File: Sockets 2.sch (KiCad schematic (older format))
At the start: 17 parts, among them J18 TABLE SENSOR, J19 PHOTO SENSOR EMITER, J20 PHOTO SENSOR RECEIVER, Q5 BC817, Q6 BC817

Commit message: Shematic almost finished, BOM in KiCad 3/4 finished
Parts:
- C60: renamed from 1nF1; value C -> 1nF; footprint (none) -> Capacitor_SMD:C_0603_1608Metric
- C61: renamed from 1nF2; value C -> 1nF; footprint (none) -> Capacitor_SMD:C_0603_1608Metric
- D27, D28: Cena (none) -> 0.14905; Link (none) -> https://www.tme.eu/pl/details/1n4448ws-7-f/diody-uniwersaln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; Model (none) -> 1N4448WS-7-F; Opis (none) -> Dioda: prostownicza; SMD; 75V; 0,25A; 4ns;; Producent (none) -> DIODES INCORPORATED; Typ (none) -> SMD
- F4, F5: Cena (none) -> 0.3763; Link (none) -> https://www.tme.eu/pl/details/sn010-60/bezpieczniki-polimer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; Model (none) -> SN010-60; Opis (none) -> Bezpiecznik: polimerowy PTC; 100mA; Obud: 1206; Producent (none) -> ECE; Typ (none) -> SMD
- J18, J20: footprint Connector_JST:JST_PH_B2B-PH-K_1x03_P2.00mm_Vertical -> Connector_JST:JST_PH_B3B-PH-K_1x03_P2.00mm_Vertical; Cena (none) -> 0.59599; Link (none) -> https://www.tme.eu/pl/details/b3b-ph-k-s/zlacza-sygnalowe-r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; Model (none) -> B3B-PH-K-S; Opis (none) -> Gniazdo; przewód-płytka; męskie; PH; 2mm; PIN: 3; THT; 100V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; Producent (none) -> JST; Typ (none) -> THT
- J19: Cena (none) -> 0.47429; Link (none) -> https://www.tme.eu/pl/details/b2b-ph-k-s/zlacza-sygnalowe-r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; Model (none) -> B2B-PH-K-S; Opis (none) -> Gniazdo; przewód-płytka; męskie; PH; 2mm; PIN: 2; THT; 100V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; Producent (none) -> JST; Typ (none) -> THT
- renumbered R50 to R49, R53 to R50, R54 to R52, R49 to R53, R52 to R54
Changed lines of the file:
@@
 F 0 "J18" H 1122 1724 50  0000 R CNN
 F 1 "TABLE SENSOR" H 1350 1900 50  0000 R CNN
-F 2 "Connector_JST:JST_PH_B2B-PH-K_1x03_P2.00mm_Vertical" H 1150 1700 50  0001 C CNN
+F 2 "Connector_JST:JST_PH_B3B-PH-K_1x03_P2.00mm_Vertical" H 1150 1700 50  0001 C CNN
 F 3 "~" H 1150 1700 50  0001 C CNN
+F 4 "0.59599" H 1150 1700 50  0001 C CNN "Cena"
+F 5 "https://www.tme.eu/pl/details/b3b-ph-k-s/zlacza-sygnalowe-raster-2-00mm/jst/" H 1150 1700 50  0001 C CNN "Link"
+F 6 "B3B-PH-K-S" H 1150 1700 50  0001 C CNN "Model"
+F 7 "Gniazdo; przewód-płytka; męskie; PH; 2mm; PIN: 3; THT; 100V; 2A" H 1150 1700 50  0001 C CNN "Opis"
+F 8 "JST" H 1150 1700 50  0001 C CNN "Producent"
+F 9 "THT" H 1150 1700 50  0001 C CNN "Typ"
 	1    1150 1700
 	1    0    0    -1
@@
 P 2450 1050
 AR Path="/5E07245F/5E173AD0" Ref="#PWR?"  Part="1"
-AR Path="/5E858220/5E173AD0" Ref="#PWR0131"  Part="1"
-F 0 "#PWR0131" H 2250 900 50  0001 C CNN
+AR Path="/5E858220/5E173AD0" Ref="#PWR0133"  Part="1"
+F 0 "#PWR0133" H 2250 900 50  0001 C CNN
 F 1 "VS" H 2467 1223 50  0000 C CNN
 F 2 "" H 2450 1050 50  0001 C CNN
@@
 F 2 "Fuse:Fuse_1206_3216Metric" H 2200 1050 50  0001 L CNN
 F 3 "~" H 2150 1250 50  0001 C CNN
+F 4 "0.3763" H 2150 1250 50  0001 C CNN "Cena"
+F 5 "https://www.tme.eu/pl/details/sn010-60/bezpieczniki-polimerowe-smd/ece/" H 2150 1250 50  0001 C CNN "Link"
+F 6 "SN010-60" H 2150 1250 50  0001 C CNN "Model"
+F 7 "Bezpiecznik: polimerowy PTC; 100mA; Obud: 1206" H 2150 1250 50  0001 C CNN "Opis"
+F 8 "ECE" H 2150 1250 50  0001 C CNN "Producent"
+F 9 "SMD" H 2150 1250 50  0001 C CNN "Typ"
 	1    2150 1250
 	0    1    1    0
@@
 P 1500 1900
 AR Path="/5E07245F/5E17A8E3" Ref="#PWR?"  Part="1"
-AR Path="/5E858220/5E17A8E3" Ref="#PWR0133"  Part="1"
-F 0 "#PWR0133" H 1500 1650 50  0001 C CNN
+AR Path="/5E858220/5E17A8E3" Ref="#PWR0131"  Part="1"
+F 0 "#PWR0131" H 1500 1650 50  0001 C CNN
 F 1 "GND" H 1505 1727 50  0000 C CNN
 F 2 "" H 1500 1900 50  0001 C CNN
@@
 P 1800 1450
 AR Path="/5E07245F/5E17BAB2" Ref="R?"  Part="1"
-AR Path="/5E858220/5E17BAB2" Ref="R50"  Part="1"
-F 0 "R50" H 1650 1500 50  0000 C CNN
+AR Path="/5E858220/5E17BAB2" Ref="R49"  Part="1"
+F 0 "R49" H 1650 1500 50  0000 C CNN
 F 1 "10kΩ" H 1650 1400 50  0000 C CNN
 F 2 "Resistor_SMD:R_0603_1608Metric" V 1730 1450 50  0001 C CNN
@@
 F 2 "Diode_SMD:D_SOD-323" H 2650 1900 50  0001 C CNN
 F 3 "~" H 2650 1900 50  0001 C CNN
+F 4 "0.14905" H 2650 1900 50  0001 C CNN "Cena"
+F 5 "https://www.tme.eu/pl/details/1n4448ws-7-f/diody-uniwersalne-smd/diodes-incorporated/" H 2650 1900 50  0001 C CNN "Link"
+F 6 "1N4448WS-7-F" H 2650 1900 50  0001 C CNN "Model"
+F 7 "Dioda: prostownicza; SMD; 75V; 0,25A; 4ns;" H 2650 1900 50  0001 C CNN "Opis"
+F 8 "DIODES INCORPORATED" H 2650 1900 50  0001 C CNN "Producent"
+F 9 "SMD" H 2650 1900 50  0001 C CNN "Typ"
 	1    2650 1900
 	0    1    1    0
@@
 P 3000 2150
 AR Path="/5E07245F/5E18427F" Ref="#PWR?"  Part="1"
-AR Path="/5E858220/5E18427F" Ref="#PWR0134"  Part="1"
-F 0 "#PWR0134" H 3000 1900 50  0001 C CNN
+AR Path="/5E858220/5E18427F" Ref="#PWR0136"  Part="1"
+F 0 "#PWR0136" H 3000 1900 50  0001 C CNN
 F 1 "GND" H 3005 1977 50  0000 C CNN
 F 2 "" H 3000 2150 50  0001 C CNN
@@
 P 3000 1250
 AR Path="/5E07245F/5E185B5B" Ref="R?"  Part="1"
-AR Path="/5E858220/5E185B5B" Ref="R49"  Part="1"
-F 0 "R49" H 2850 1300 50  0000 C CNN
+AR Path="/5E858220/5E185B5B" Ref="R53"  Part="1"
+F 0 "R53" H 2850 1300 50  0000 C CNN
 F 1 "10kΩ" H 2850 1200 50  0000 C CNN
 F 2 "Resistor_SMD:R_0603_1608Metric" V 2930 1250 50  0001 C CNN
@@
 $EndComp
 $Comp
-L power:+3.3V #PWR0132
+L power:+3.3V #PWR0135
 U 1 1 5E187914
 P 3000 1050
-F 0 "#PWR0132" H 3000 900 50  0001 C CNN
+F 0 "#PWR0135" H 3000 900 50  0001 C CNN
 F 1 "+3.3V" H 3015 1223 50  0000 C CNN
 F 2 "" H 3000 1050 50  0001 C CNN
@@
 NPN NC
 $Comp
-L Device:C 1nF1
+L Device:C C60
 U 1 1 5E189FA4
 P 3550 1700
-F 0 "1nF1" H 3665 1746 50  0000 L CNN
-F 1 "C" H 3665 1655 50  0000 L CNN
-F 2 "" H 3588 1550 50  0001 C CNN
+F 0 "C60" H 3665 1746 50  0000 L CNN
+F 1 "1nF" H 3665 1655 50  0000 L CNN
+F 2 "Capacitor_SMD:C_0603_1608Metric" H 3588 1550 50  0001 C CNN
 F 3 "~" H 3550 1700 50  0001 C CNN
 	1    3550 1700
@@
 F 0 "J20" H 1372 3874 50  0000 R CNN
 F 1 "PHOTO SENSOR RECEIVER" H 1600 4050 50  0000 R CNN
-F 2 "Connector_JST:JST_PH_B2B-PH-K_1x03_P2.00mm_Vertical" H 1400 3850 50  0001 C CNN
+F 2 "Connector_JST:JST_PH_B3B-PH-K_1x03_P2.00mm_Vertical" H 1400 3850 50  0001 C CNN
 F 3 "~" H 1400 3850 50  0001 C CNN
+F 4 "0.59599" H 1400 3850 50  0001 C CNN "Cena"
+F 5 "https://www.tme.eu/pl/details/b3b-ph-k-s/zlacza-sygnalowe-raster-2-00mm/jst/" H 1400 3850 50  0001 C CNN "Link"
+F 6 "B3B-PH-K-S" H 1400 3850 50  0001 C CNN "Model"
+F 7 "Gniazdo; przewód-płytka; męskie; PH; 2mm; PIN: 3; THT; 100V; 2A" H 1400 3850 50  0001 C CNN "Opis"
+F 8 "JST" H 1400 3850 50  0001 C CNN "Producent"
+F 9 "THT" H 1400 3850 50  0001 C CNN "Typ"
 	1    1400 3850
 	1    0    0    -1
@@
 P 2550 2850
 AR Path="/5E07245F/5E1B90F7" Ref="#PWR?"  Part="1"
-AR Path="/5E858220/5E1B90F7" Ref="#PWR0135"  Part="1"
-F 0 "#PWR0135" H 2350 2700 50  0001 C CNN
+AR Path="/5E858220/5E1B90F7" Ref="#PWR0134"  Part="1"
+F 0 "#PWR0134" H 2350 2700 50  0001 C CNN
 F 1 "VS" H 2567 3023 50  0000 C CNN
 F 2 "" H 2550 2850 50  0001 C CNN
@@
 F 2 "Fuse:Fuse_1206_3216Metric" H 2250 2800 50  0001 L CNN
 F 3 "~" H 2200 3000 50  0001 C CNN
+F 4 "0.3763" H 2200 3000 50  0001 C CNN "Cena"
+F 5 "https://www.tme.eu/pl/details/sn010-60/bezpieczniki-polimerowe-smd/ece/" H 2200 3000 50  0001 C CNN "Link"
+F 6 "SN010-60" H 2200 3000 50  0001 C CNN "Model"
+F 7 "Bezpiecznik: polimerowy PTC; 100mA; Obud: 1206" H 2200 3000 50  0001 C CNN "Opis"
+F 8 "ECE" H 2200 3000 50  0001 C CNN "Producent"
+F 9 "SMD" H 2200 3000 50  0001 C CNN "Typ"
 	1    2200 3000
 	0    1    1    0
@@
 P 1700 4050
 AR Path="/5E07245F/5E1B910F" Ref="#PWR?"  Part="1"
-AR Path="/5E858220/5E1B910F" Ref="#PWR0137"  Part="1"
-F 0 "#PWR0137" H 1700 3800 50  0001 C CNN
+AR Path="/5E858220/5E1B910F" Ref="#PWR0132"  Part="1"
+F 0 "#PWR0132" H 1700 3800 50  0001 C CNN
 F 1 "GND" H 1705 3877 50  0000 C CNN
 F 2 "" H 1700 4050 50  0001 C CNN
@@
 P 2050 3450
 AR Path="/5E07245F/5E1B911B" Ref="R?"  Part="1"
-AR Path="/5E858220/5E1B911B" Ref="R53"  Part="1"
-F 0 "R53" H 2150 3500 50  0000 C CNN
+AR Path="/5E858220/5E1B911B" Ref="R50"  Part="1"
+F 0 "R50" H 2150 3500 50  0000 C CNN
 F 1 "10kΩ" H 2200 3400 50  0000 C CNN
 F 2 "Resistor_SMD:R_0603_1608Metric" V 1980 3450 50  0001 C CNN
@@
 P 2350 3850
 AR Path="/5E07245F/5E1B9135" Ref="R?"  Part="1"
-AR Path="/5E858220/5E1B9135" Ref="R54"  Part="1"
-F 0 "R54" V 2150 3850 50  0000 C CNN
+AR Path="/5E858220/5E1B9135" Ref="R52"  Part="1"
+F 0 "R52" V 2150 3850 50  0000 C CNN
 F 1 "33kΩ" V 2250 3850 50  0000 C CNN
 F 2 "Resistor_SMD:R_0603_1608Metric" V 2280 3850 50  0001 C CNN
@@
 F 2 "Diode_SMD:D_SOD-323" H 2900 4050 50  0001 C CNN
 F 3 "~" H 2900 4050 50  0001 C CNN
+F 4 "0.14905" H 2900 4050 50  0001 C CNN "Cena"
+F 5 "https://www.tme.eu/pl/details/1n4448ws-7-f/diody-uniwersalne-smd/diodes-incorporated/" H 2900 4050 50  0001 C CNN "Link"
+F 6 "1N4448WS-7-F" H 2900 4050 50  0001 C CNN "Model"
+F 7 "Dioda: prostownicza; SMD; 75V; 0,25A; 4ns;" H 2900 4050 50  0001 C CNN "Opis"
+F 8 "DIODES INCORPORATED" H 2900 4050 50  0001 C CNN "Producent"
+F 9 "SMD" H 2900 4050 50  0001 C CNN "Typ"
 	1    2900 4050
 	0    1    1    0
@@
 P 3250 3400
 AR Path="/5E07245F/5E1B915B" Ref="R?"  Part="1"
-AR Path="/5E858220/5E1B915B" Ref="R52"  Part="1"
-F 0 "R52" H 3100 3450 50  0000 C CNN
+AR Path="/5E858220/5E1B915B" Ref="R54"  Part="1"
+F 0 "R54" H 3100 3450 50  0000 C CNN
 F 1 "10kΩ" H 3100 3350 50  0000 C CNN
 F 2 "Resistor_SMD:R_0603_1608Metric" V 3180 3400 50  0001 C CNN
@@
 $EndComp
 $Comp
-L power:+3.3V #PWR0136
+L power:+3.3V #PWR0137
 U 1 1 5E1B9165
 P 3250 3200
-F 0 "#PWR0136" H 3250 3050 50  0001 C CNN
+F 0 "#PWR0137" H 3250 3050 50  0001 C CNN
 F 1 "+3.3V" H 3265 3373 50  0000 C CNN
 F 2 "" H 3250 3200 50  0001 C CNN
@@
 NPN NC
 $Comp
-L Device:C 1nF2
+L Device:C C61
 U 1 1 5E1B9175
 P 3800 3850
-F 0 "1nF2" H 3915 3896 50  0000 L CNN
-F 1 "C" H 3915 3805 50  0000 L CNN
-F 2 "" H 3838 3700 50  0001 C CNN
+F 0 "C61" H 3915 3896 50  0000 L CNN
+F 1 "1nF" H 3915 3805 50  0000 L CNN
+F 2 "Capacitor_SMD:C_0603_1608Metric" H 3838 3700 50  0001 C CNN
 F 3 "~" H 3800 3850 50  0001 C CNN
 	1    3800 3850
@@
 F 2 "Connector_JST:JST_PH_B2B-PH-K_1x02_P2.00mm_Vertical" H 1400 3000 50  0001 C CNN
 F 3 "~" H 1400 3000 50  0001 C CNN
+F 4 "0.47429" H 1400 3000 50  0001 C CNN "Cena"
+F 5 "https://www.tme.eu/pl/details/b2b-ph-k-s/zlacza-sygnalowe-raster-2-00mm/jst/" H 1400 3000 50  0001 C CNN "Link"
+F 6 "B2B-PH-K-S" H 1400 3000 50  0001 C CNN "Model"
+F 7 "Gniazdo; przewód-płytka; męskie; PH; 2mm; PIN: 2; THT; 100V; 2A" H 1400 3000 50  0001 C CNN "Opis"
+F 8 "JST" H 1400 3000 50  0001 C CNN "Producent"
+F 9 "THT" H 1400 3000 50  0001 C CNN "Typ"
 	1    1400 3000
 	1    0    0    -1

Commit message: BOM in KiCad almost finished, genereated NETLIST, create PCB
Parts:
- C60, C61: Cena (none) -> 0.05563; Link (none) -> https://www.tme.eu/pl/details/cl10b102kb8nnnc/kondensatory-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; Model (none) -> CL10B102KB8NNNC; Opis (none) -> Kondensator: ceramiczny; MLCC; 1nF; 50V; X7R; ±10%; SMD; 06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; Producent (none) -> SAMSUNG; Typ (none) -> SMD
- Q5, Q6: Cena (none) -> 0.1189; Link (none) -> https://www.tme.eu/pl/details/bc817.215/tranzystory-npn-smd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; Model (none) -> BC817.215; Opis (none) -> Tranzystor: NPN; bipolarny; 45V; 0,5A; 250mW; SOT23; Producent (none) -> NEXPERIA; Typ (none) -> SMD
- R49, R50, R53, R54: Cena (none) -> 0.03622; Link (none) -> https://www.tme.eu/pl/details/smd0603-10k-1%25/rezystory-sm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; Model (none) -> 0603SAF1002T5E; Opis (none) -> Rezystor: thick film; SMD; 0603; 10kΩ; 0,1W; ±1%; -55÷155°C; Producent (none) -> ROYAL OHM; Typ (none) -> SMD
- R51, R52: Cena (none) -> 0.04651; Typ (none) -> SMD
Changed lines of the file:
@@
 F 2 "Resistor_SMD:R_0603_1608Metric" V 1730 1450 50  0001 C CNN
 F 3 "~" H 1800 1450 50  0001 C CNN
+F 4 "0.03622" H 1800 1450 50  0001 C CNN "Cena"
+F 5 "https://www.tme.eu/pl/details/smd0603-10k-1%25/rezystory-smd-0603/royal-ohm/0603saf1002t5e/" H 1800 1450 50  0001 C CNN "Link"
+F 6 "0603SAF1002T5E" H 1800 1450 50  0001 C CNN "Model"
+F 7 "Rezystor: thick film; SMD; 0603; 10kΩ; 0,1W; ±1%; -55÷155°C" H 1800 1450 50  0001 C CNN "Opis"
+F 8 "ROYAL OHM" H 1800 1450 50  0001 C CNN "Producent"
+F 9 "SMD" H 1800 1450 50  0001 C CNN "Typ"
 	1    1800 1450
 	1    0    0    -1
@@
 F 2 "Package_TO_SOT_SMD:SOT-23" H 3100 1625 50  0001 L CIN
 F 3 "http://www.fairchildsemi.com/ds/BC/BC817.pdf" H 2900 1700 50  0001 L CNN
+F 4 "0.1189" H 2900 1700 50  0001 C CNN "Cena"
+F 5 "https://www.tme.eu/pl/details/bc817.215/tranzystory-npn-smd/nexperia/" H 2900 1700 50  0001 C CNN "Link"
+F 6 "BC817.215" H 2900 1700 50  0001 C CNN "Model"
+F 7 "Tranzystor: NPN; bipolarny; 45V; 0,5A; 250mW; SOT23" H 2900 1700 50  0001 C CNN "Opis"
+F 8 "NEXPERIA" H 2900 1700 50  0001 C CNN "Producent"
+F 9 "SMD" H 2900 1700 50  0001 C CNN "Typ"
 	1    2900 1700
 	1    0    0    -1
@@
 F 2 "Resistor_SMD:R_0603_1608Metric" V 2030 1700 50  0001 C CNN
 F 3 "~" H 2100 1700 50  0001 C CNN
+F 4 "0.04651" H 2100 1700 50  0001 C CNN "Cena"
+F 5 "SMD" H 2100 1700 50  0001 C CNN "Typ"
 	1    2100 1700
 	0    1    1    0
@@
 F 2 "Resistor_SMD:R_0603_1608Metric" V 2930 1250 50  0001 C CNN
 F 3 "~" H 3000 1250 50  0001 C CNN
+F 4 "0.03622" H 3000 1250 50  0001 C CNN "Cena"
+F 5 "https://www.tme.eu/pl/details/smd0603-10k-1%25/rezystory-smd-0603/royal-ohm/0603saf1002t5e/" H 3000 1250 50  0001 C CNN "Link"
+F 6 "0603SAF1002T5E" H 3000 1250 50  0001 C CNN "Model"
+F 7 "Rezystor: thick film; SMD; 0603; 10kΩ; 0,1W; ±1%; -55÷155°C" H 3000 1250 50  0001 C CNN "Opis"
+F 8 "ROYAL OHM" H 3000 1250 50  0001 C CNN "Producent"
+F 9 "SMD" H 3000 1250 50  0001 C CNN "Typ"
 	1    3000 1250
 	1    0    0    -1
@@
 F 2 "Capacitor_SMD:C_0603_1608Metric" H 3588 1550 50  0001 C CNN
 F 3 "~" H 3550 1700 50  0001 C CNN
+F 4 "0.05563" H 3550 1700 50  0001 C CNN "Cena"
+F 5 "https://www.tme.eu/pl/details/cl10b102kb8nnnc/kondensatory-mlcc-smd-0603/samsung/" H 3550 1700 50  0001 C CNN "Link"
+F 6 "CL10B102KB8NNNC" H 3550 1700 50  0001 C CNN "Model"
+F 7 "Kondensator: ceramiczny; MLCC; 1nF; 50V; X7R; ±10%; SMD; 0603" H 3550 1700 50  0001 C CNN "Opis"
+F 8 "SAMSUNG" H 3550 1700 50  0001 C CNN "Producent"
+F 9 "SMD" H 3550 1700 50  0001 C CNN "Typ"
 	1    3550 1700
 	1    0    0    -1
@@
 F 2 "Resistor_SMD:R_0603_1608Metric" V 1980 3450 50  0001 C CNN
 F 3 "~" H 2050 3450 50  0001 C CNN
+F 4 "0.03622" H 2050 3450 50  0001 C CNN "Cena"
+F 5 "https://www.tme.eu/pl/details/smd0603-10k-1%25/rezystory-smd-0603/royal-ohm/0603saf1002t5e/" H 2050 3450 50  0001 C CNN "Link"
+F 6 "0603SAF1002T5E" H 2050 3450 50  0001 C CNN "Model"
+F 7 "Rezystor: thick film; SMD; 0603; 10kΩ; 0,1W; ±1%; -55÷155°C" H 2050 3450 50  0001 C CNN "Opis"
+F 8 "ROYAL OHM" H 2050 3450 50  0001 C CNN "Producent"
+F 9 "SMD" H 2050 3450 50  0001 C CNN "Typ"
 	1    2050 3450
 	1    0    0    -1
@@
 F 2 "Package_TO_SOT_SMD:SOT-23" H 3350 3775 50  0001 L CIN
 F 3 "http://www.fairchildsemi.com/ds/BC/BC817.pdf" H 3150 3850 50  0001 L CNN
+F 4 "0.1189" H 3150 3850 50  0001 C CNN "Cena"
+F 5 "https://www.tme.eu/pl/details/bc817.215/tranzystory-npn-smd/nexperia/" H 3150 3850 50  0001 C CNN "Link"
+F 6 "BC817.215" H 3150 3850 50  0001 C CNN "Model"
+F 7 "Tranzystor: NPN; bipolarny; 45V; 0,5A; 250mW; SOT23" H 3150 3850 50  0001 C CNN "Opis"
+F 8 "NEXPERIA" H 3150 3850 50  0001 C CNN "Producent"
+F 9 "SMD" H 3150 3850 50  0001 C CNN "Typ"
 	1    3150 3850
 	1    0    0    -1
@@
 F 2 "Resistor_SMD:R_0603_1608Metric" V 2280 3850 50  0001 C CNN
 F 3 "~" H 2350 3850 50  0001 C CNN
+F 4 "0.04651" H 2350 3850 50  0001 C CNN "Cena"
+F 5 "SMD" H 2350 3850 50  0001 C CNN "Typ"
 	1    2350 3850
 	0    1    1    0
@@
 F 2 "Resistor_SMD:R_0603_1608Metric" V 3180 3400 50  0001 C CNN
 F 3 "~" H 3250 3400 50  0001 C CNN
+F 4 "0.03622" H 3250 3400 50  0001 C CNN "Cena"
+F 5 "https://www.tme.eu/pl/details/smd0603-10k-1%25/rezystory-smd-0603/royal-ohm/0603saf1002t5e/" H 3250 3400 50  0001 C CNN "Link"
+F 6 "0603SAF1002T5E" H 3250 3400 50  0001 C CNN "Model"
+F 7 "Rezystor: thick film; SMD; 0603; 10kΩ; 0,1W; ±1%; -55÷155°C" H 3250 3400 50  0001 C CNN "Opis"
+F 8 "ROYAL OHM" H 3250 3400 50  0001 C CNN "Producent"
+F 9 "SMD" H 3250 3400 50  0001 C CNN "Typ"
 	1    3250 3400
 	1    0    0    -1
@@
 F 2 "Capacitor_SMD:C_0603_1608Metric" H 3838 3700 50  0001 C CNN
 F 3 "~" H 3800 3850 50  0001 C CNN
+F 4 "0.05563" H 3800 3850 50  0001 C CNN "Cena"
+F 5 "https://www.tme.eu/pl/details/cl10b102kb8nnnc/kondensatory-mlcc-smd-0603/samsung/" H 3800 3850 50  0001 C CNN "Link"
+F 6 "CL10B102KB8NNNC" H 3800 3850 50  0001 C CNN "Model"
+F 7 "Kondensator: ceramiczny; MLCC; 1nF; 50V; X7R; ±10%; SMD; 0603" H 3800 3850 50  0001 C CNN "Opis"
+F 8 "SAMSUNG" H 3800 3850 50  0001 C CNN "Producent"
+F 9 "SMD" H 3800 3850 50  0001 C CNN "Typ"
 	1    3800 3850
 	1    0    0    -1

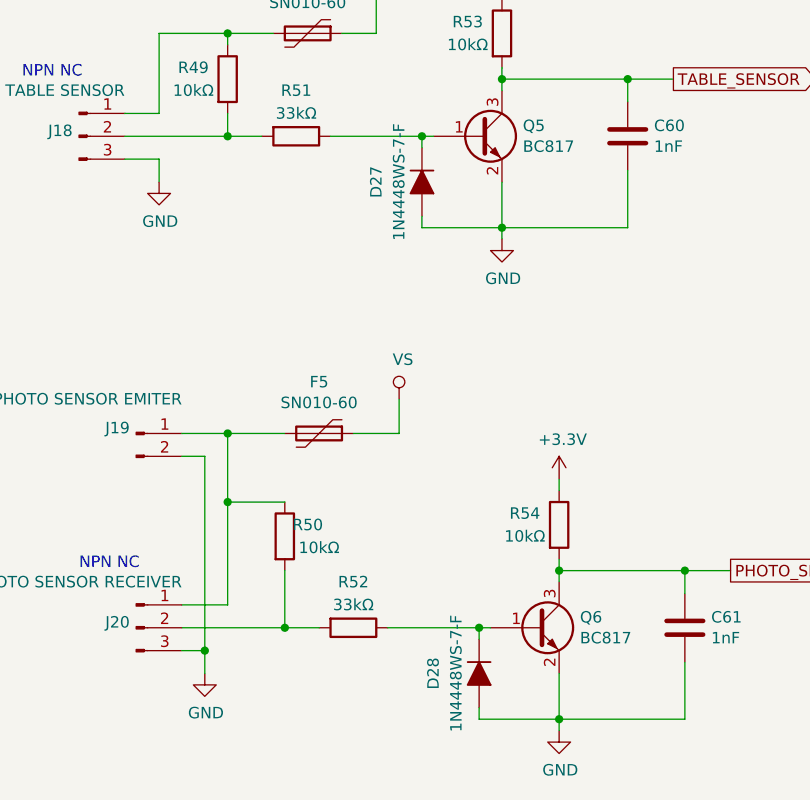
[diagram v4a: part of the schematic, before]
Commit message: Improve Emergency, Added TVS diodes
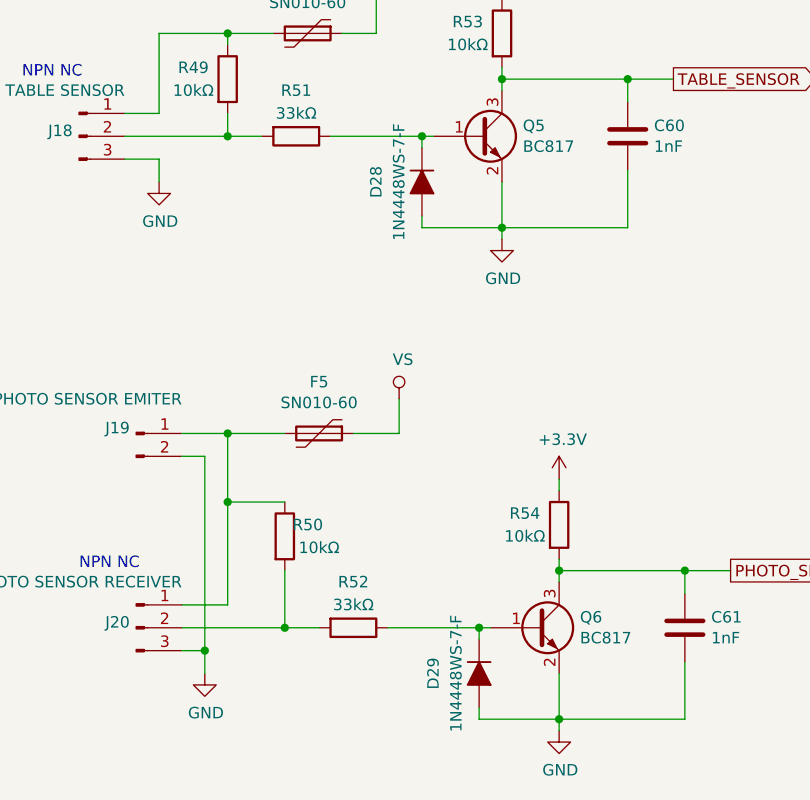
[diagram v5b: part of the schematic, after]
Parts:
- renumbered D27 to D28, D28 to D29
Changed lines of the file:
@@
 AR Path="/5E1018C2/5E182EF0" Ref="D?"  Part="1"
 AR Path="/5E91D7CC/5E182EF0" Ref="D?"  Part="1"
-AR Path="/5E858220/5E182EF0" Ref="D27"  Part="1"
-F 0 "D27" H 2650 1700 50  0000 C CNN
+AR Path="/5E858220/5E182EF0" Ref="D28"  Part="1"
+F 0 "D28" H 2650 1700 50  0000 C CNN
 F 1 "1N4448WS-7-F" H 2650 1800 50  0000 C CNN
 F 2 "Diode_SMD:D_SOD-323" H 2650 1900 50  0001 C CNN
@@
 AR Path="/5E1018C2/5E1B9141" Ref="D?"  Part="1"
 AR Path="/5E91D7CC/5E1B9141" Ref="D?"  Part="1"
-AR Path="/5E858220/5E1B9141" Ref="D28"  Part="1"
-F 0 "D28" H 2900 3850 50  0000 C CNN
+AR Path="/5E858220/5E1B9141" Ref="D29"  Part="1"
+F 0 "D29" H 2900 3850 50  0000 C CNN
 F 1 "1N4448WS-7-F" H 2900 3950 50  0000 C CNN
 F 2 "Diode_SMD:D_SOD-323" H 2900 4050 50  0001 C CNN
